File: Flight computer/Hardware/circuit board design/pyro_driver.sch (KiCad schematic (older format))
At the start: 7 parts, among them J4 Conn_01x06_Female, U5 LM2903, U6 Si7232DN

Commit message: worked on the silabs 4463 radio chip
- filled in the component values for TX matching and tx filtering
- filled in tentative values for RX LNA matching. Will have to verify
- swapped out XTAL and put in an RS Pro TCXO. Decoupled its powersupply.
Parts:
- R3: value 3.3 -> 3.3K
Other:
- moved on the sheet: R3, R4, R5, R6, U5A
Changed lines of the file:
@@
 $Descr A4 11693 8268
 encoding utf-8
-Sheet 7 7
+Sheet 6 7
 Title "Pyro drivers"
 Date "2019-08-26"
@@
 L Comparator:LM2903 U5
 U 1 1 5D6C6230
-P 3050 1550
-F 0 "U5" H 3050 1917 50  0000 C CNN
-F 1 "LM2903" H 3050 1826 50  0000 C CNN
-F 2 "" H 3050 1550 50  0001 C CNN
-F 3 "http://www.ti.com/lit/ds/symlink/lm393-n.pdf" H 3050 1550 50  0001 C CNN
-	1    3050 1550
+P 2700 1200
+F 0 "U5" H 2700 1567 50  0000 C CNN
+F 1 "LM2903" H 2700 1476 50  0000 C CNN
+F 2 "" H 2700 1200 50  0001 C CNN
+F 3 "http://www.ti.com/lit/ds/symlink/lm393-n.pdf" H 2700 1200 50  0001 C CNN
+	1    2700 1200
 	1    0    0    -1
 $EndComp
@@
 L Driver_FET:Si7232DN U6
 U 1 1 5D696EFB
-P 4400 1500
-F 0 "U6" H 4506 1046 50  0000 L CNN
-F 1 "Si7232DN" H 4506 955 50  0000 L CNN
-F 2 "Package_SO:Vishay_PowerPAK_1212-8_Dual" H 4250 1750 50  0001 C CNN
-F 3 "https://www.vishay.com/docs/68986/si7232dn.pdf" H 4400 1500 50  0001 C CNN
-	1    4400 1500
+P 4050 1150
+F 0 "U6" H 4156 696 50  0000 L CNN
+F 1 "Si7232DN" H 4156 605 50  0000 L CNN
+F 2 "Package_SO:Vishay_PowerPAK_1212-8_Dual" H 3900 1400 50  0001 C CNN
+F 3 "https://www.vishay.com/docs/68986/si7232dn.pdf" H 4050 1150 50  0001 C CNN
+	1    4050 1150
 	1    0    0    -1
 $EndComp
@@
 L power:GND #PWR024
 U 1 1 5D69AE81
-P 4400 2400
-F 0 "#PWR024" H 4400 2150 50  0001 C CNN
-F 1 "GND" H 4405 2227 50  0000 C CNN
-F 2 "" H 4400 2400 50  0001 C CNN
-F 3 "" H 4400 2400 50  0001 C CNN
-	1    4400 2400
-	1    0    0    -1
-$EndComp
-Wire Wire Line
-	4400 2400 4400 2150
+P 4050 2050
+F 0 "#PWR024" H 4050 1800 50  0001 C CNN
+F 1 "GND" H 4055 1877 50  0000 C CNN
+F 2 "" H 4050 2050 50  0001 C CNN
+F 3 "" H 4050 2050 50  0001 C CNN
+	1    4050 2050
+	1    0    0    -1
+$EndComp
+Wire Wire Line
+	4050 2050 4050 1800
 $Comp
 L Device:R R5
 U 1 1 5D6A50BE
-P 5050 1750
-F 0 "R5" V 5250 1750 50  0000 C CNN
-F 1 "100K" V 5150 1750 50  0000 C CNN
-F 2 "" V 4980 1750 50  0001 C CNN
-F 3 "~" H 5050 1750 50  0001 C CNN
-	1    5050 1750
+P 4700 1400
+F 0 "R5" V 4900 1400 50  0000 C CNN
+F 1 "100K" V 4800 1400 50  0000 C CNN
+F 2 "" V 4630 1400 50  0001 C CNN
+F 3 "~" H 4700 1400 50  0001 C CNN
+	1    4700 1400
 	0    1    1    0
 $EndComp
@@
 L Device:R R6
 U 1 1 5D6A6316
-P 5500 2200
-F 0 "R6" H 5570 2246 50  0000 L CNN
-F 1 "27K" H 5570 2155 50  0000 L CNN
-F 2 "" V 5430 2200 50  0001 C CNN
-F 3 "~" H 5500 2200 50  0001 C CNN
-	1    5500 2200
-	1    0    0    -1
-$EndComp
-Wire Wire Line
-	5200 1750 5500 1750
-Wire Wire Line
-	5500 2050 5500 1750
-Wire Wire Line
-	5500 2400 5500 2350
+P 5150 1850
+F 0 "R6" H 5220 1896 50  0000 L CNN
+F 1 "27K" H 5220 1805 50  0000 L CNN
+F 2 "" V 5080 1850 50  0001 C CNN
+F 3 "~" H 5150 1850 50  0001 C CNN
+	1    5150 1850
+	1    0    0    -1
+$EndComp
+Wire Wire Line
+	4850 1400 5150 1400
+Wire Wire Line
+	5150 1700 5150 1400
+Wire Wire Line
+	5150 2050 5150 2000
 $Comp
 L power:GND #PWR025
 U 1 1 5D6A67BF
-P 5500 2400
-F 0 "#PWR025" H 5500 2150 50  0001 C CNN
-F 1 "GND" H 5505 2227 50  0000 C CNN
-F 2 "" H 5500 2400 50  0001 C CNN
-F 3 "" H 5500 2400 50  0001 C CNN
-	1    5500 2400
-	1    0    0    -1
-$EndComp
-Wire Wire Line
-	4500 1750 4700 1750
-Wire Wire Line
-	4500 1650 4700 1650
-Wire Wire Line
-	4700 1750 4700 1650
-Connection ~ 4700 1750
-Wire Wire Line
-	4700 1750 4900 1750
-Connection ~ 4700 1650
-Wire Wire Line
-	4700 1650 6000 1650
-Connection ~ 5500 1750
-Wire Wire Line
-	5500 1750 6000 1750
-Text HLabel 6000 1750 2    50   Output ~ 0
+P 5150 2050
+F 0 "#PWR025" H 5150 1800 50  0001 C CNN
+F 1 "GND" H 5155 1877 50  0000 C CNN
+F 2 "" H 5150 2050 50  0001 C CNN
+F 3 "" H 5150 2050 50  0001 C CNN
+	1    5150 2050
+	1    0    0    -1
+$EndComp
+Wire Wire Line
+	4150 1400 4350 1400
+Wire Wire Line
+	4150 1300 4350 1300
+Wire Wire Line
+	4350 1400 4350 1300
+Connection ~ 4350 1400
+Wire Wire Line
+	4350 1400 4550 1400
+Connection ~ 4350 1300
+Wire Wire Line
+	4350 1300 5650 1300
+Connection ~ 5150 1400
+Wire Wire Line
+	5150 1400 5650 1400
+Text HLabel 5650 1400 2    50   Output ~ 0
 sense_fet_a
-Text Label 6000 1650 0    50   ~ 0
+Text Label 5650 1300 0    50   ~ 0
 fet_a
 Wire Wire Line
-	3350 1550 3800 1550
-Wire Wire Line
-	3800 1550 3800 1950
-Wire Wire Line
-	3800 1950 4100 1950
-Wire Wire Line
-	3800 1950 3500 1950
-Connection ~ 3800 1950
-Wire Wire Line
-	3000 1950 3000 2100
-Connection ~ 3000 1950
-Wire Wire Line
-	3000 1950 2250 1950
+	3000 1200 3450 1200
+Wire Wire Line
+	3450 1200 3450 1600
+Wire Wire Line
+	3450 1600 3750 1600
+Wire Wire Line
+	3450 1600 3150 1600
+Connection ~ 3450 1600
+Wire Wire Line
+	2650 1600 2650 1750
+Connection ~ 2650 1600
+Wire Wire Line
+	2650 1600 1900 1600
 $Comp
 L power:GND #PWR023
 U 1 1 5D6AF664
-P 3000 2500
-F 0 "#PWR023" H 3000 2250 50  0001 C CNN
-F 1 "GND" H 3005 2327 50  0000 C CNN
-F 2 "" H 3000 2500 50  0001 C CNN
-F 3 "" H 3000 2500 50  0001 C CNN
-	1    3000 2500
+P 2650 2150
+F 0 "#PWR023" H 2650 1900 50  0001 C CNN
+F 1 "GND" H 2655 1977 50  0000 C CNN
+F 2 "" H 2650 2150 50  0001 C CNN
+F 3 "" H 2650 2150 50  0001 C CNN
+	1    2650 2150
 	1    0    0    -1
 $EndComp
@@
 L Device:R R3
 U 1 1 5D6AFE1F
-P 3000 2250
-F 0 "R3" H 3070 2296 50  0000 L CNN
-F 1 "3.3" H 3070 2205 50  0000 L CNN
-F 2 "" V 2930 2250 50  0001 C CNN
-F 3 "~" H 3000 2250 50  0001 C CNN
-	1    3000 2250
-	1    0    0    -1
-$EndComp
-Wire Wire Line
-	3000 2400 3000 2500
+P 2650 1900
+F 0 "R3" H 2720 1946 50  0000 L CNN
+F 1 "3.3K" H 2720 1855 50  0000 L CNN
+F 2 "" V 2580 1900 50  0001 C CNN
+F 3 "~" H 2650 1900 50  0001 C CNN
+	1    2650 1900
+	1    0    0    -1
+$EndComp
+Wire Wire Line
+	2650 2050 2650 2150
 $Comp
 L Device:R R4
 U 1 1 5D6B06F6
-P 3350 1950
-F 0 "R4" V 3143 1950 50  0000 C CNN
-F 1 "100" V 3234 1950 50  0000 C CNN
-F 2 "" V 3280 1950 50  0001 C CNN
-F 3 "~" H 3350 1950 50  0001 C CNN
-	1    3350 1950
+P 3000 1600
+F 0 "R4" V 2793 1600 50  0000 C CNN
+F 1 "100" V 2884 1600 50  0000 C CNN
+F 2 "" V 2930 1600 50  0001 C CNN
+F 3 "~" H 3000 1600 50  0001 C CNN
+	1    3000 1600
 	0    1    1    0
 $EndComp
 Wire Wire Line
-	3200 1950 3000 1950
-Text HLabel 2250 1950 0    50   Output ~ 0
+	2850 1600 2650 1600
+Text HLabel 1900 1600 0    50   Output ~ 0
 fire_a
 $Comp
@@
 	1    0    0    -1
 $EndComp
-NoConn ~ 2750 1650
-NoConn ~ 2750 1450
+NoConn ~ 2400 1300
+NoConn ~ 2400 1100
 NoConn ~ 1900 3900
 NoConn ~ 1900 4000

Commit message: Work in progress for Telemetry Radio
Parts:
- U6: symbol Driver_FET:Si7232DN -> circuit-board-design-rescue:Si7232DN-Driver_FET
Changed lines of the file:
@@
 $EndComp
 $Comp
-L Driver_FET:Si7232DN U6
+L circuit-board-design-rescue:Si7232DN-Driver_FET U6
 U 1 1 5D696EFB
 P 4050 1150
+AR Path="/5D696EFB" Ref="U6"  Part="1"
+AR Path="/5D6468D5/5D696EFB" Ref="U6"  Part="1"
 F 0 "U6" H 4156 696 50  0000 L CNN
 F 1 "Si7232DN" H 4156 605 50  0000 L CNN

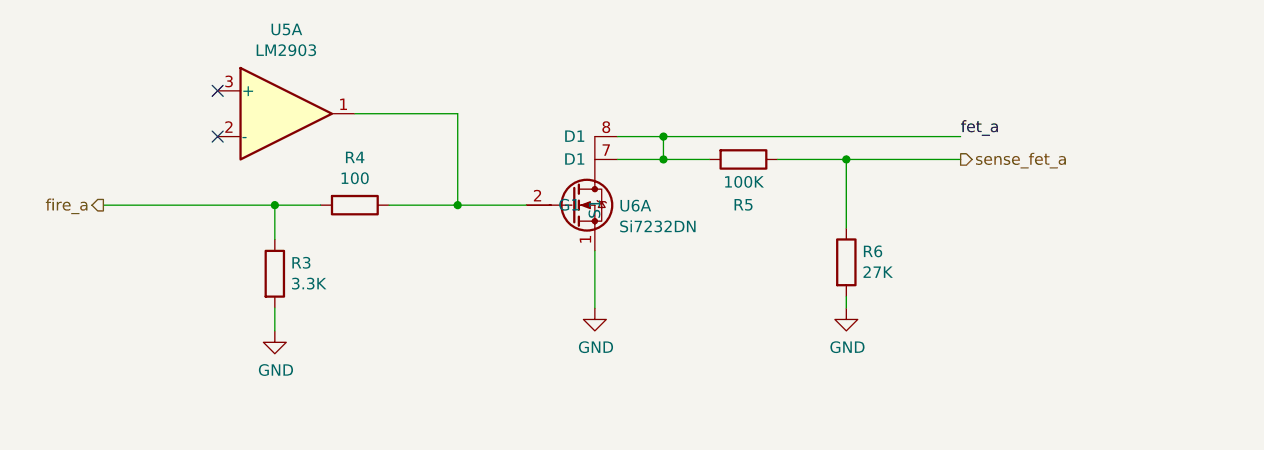
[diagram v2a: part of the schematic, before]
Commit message: changed the SPI flash chip
-changed to Winbond W74M64FV 64Mbit flash chip to run on 3.3V. Changed schematic symbol and foot print.
- changed the names of hierarchical labels for the pyros
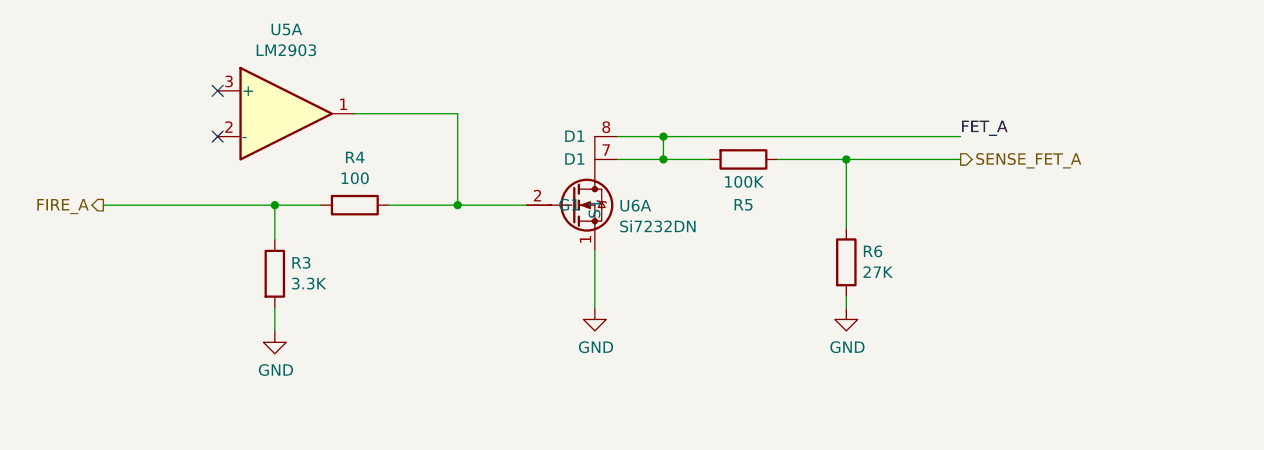
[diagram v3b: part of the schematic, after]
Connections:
- net fet_a renamed FET_A
- net fire_a renamed FIRE_A
- net sense_fet_a renamed SENSE_FET_A
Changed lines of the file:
@@
 	5150 1400 5650 1400
 Text HLabel 5650 1400 2    50   Output ~ 0
-sense_fet_a
+SENSE_FET_A
 Text Label 5650 1300 0    50   ~ 0
-fet_a
+FET_A
 Wire Wire Line
 	3000 1200 3450 1200
@@
 	2850 1600 2650 1600
 Text HLabel 1900 1600 0    50   Output ~ 0
-fire_a
+FIRE_A
 $Comp
 L power:GND #PWR027

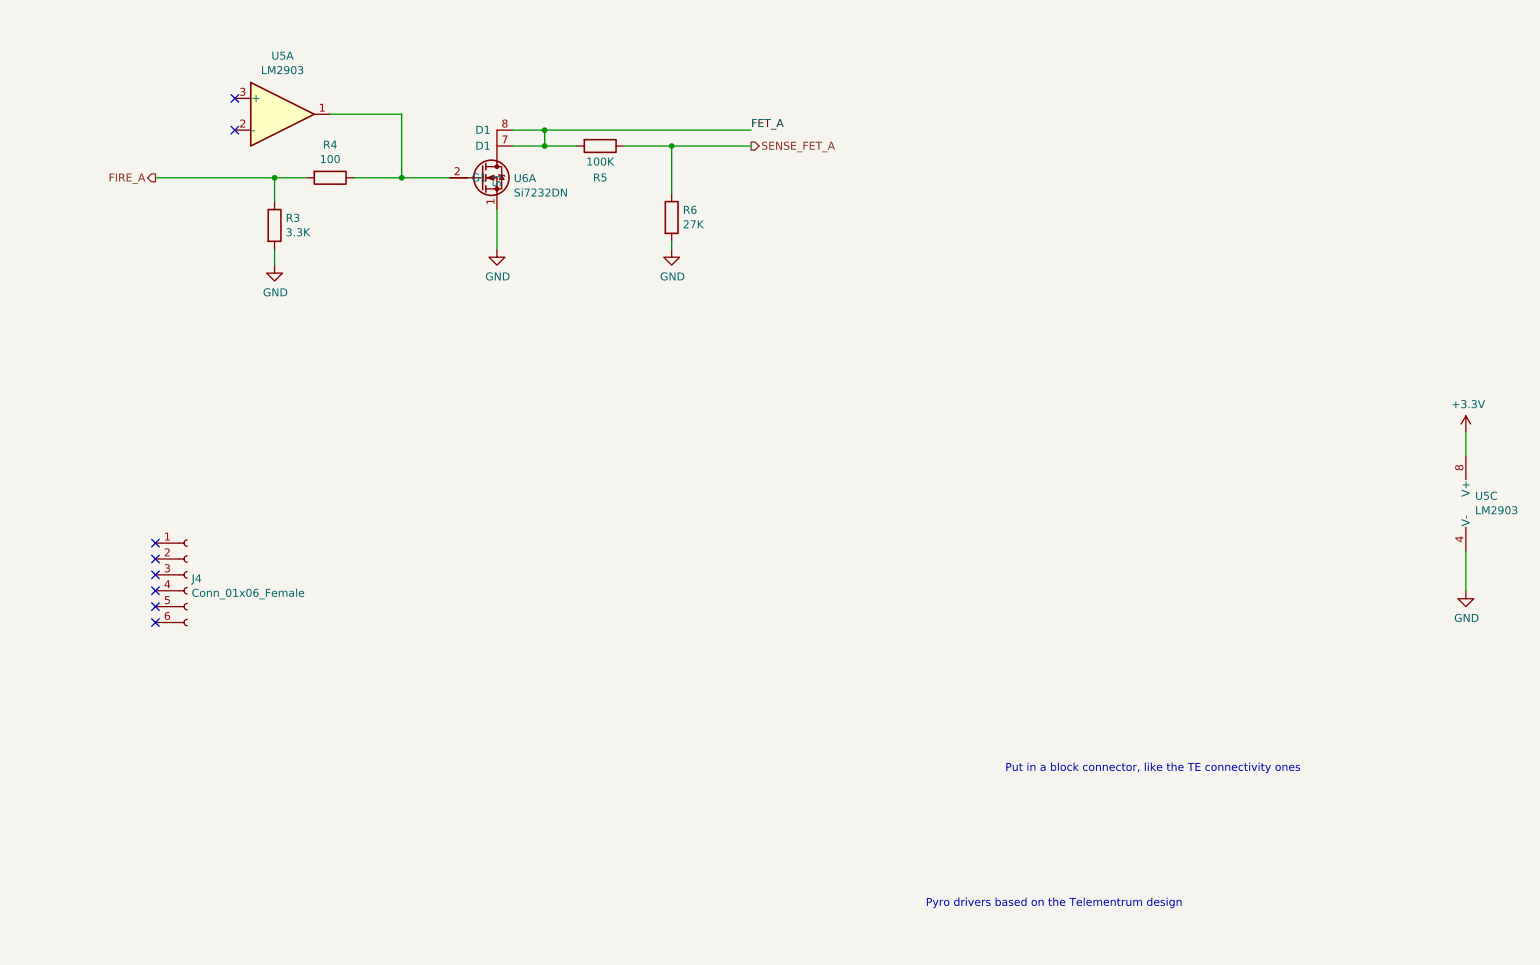
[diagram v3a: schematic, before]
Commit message: created net list for first time
-changed SAML21 to J variant7
-filled in foot prints for all components exept comparator
-changed the footprints of ICSS pico tracker to a local copy
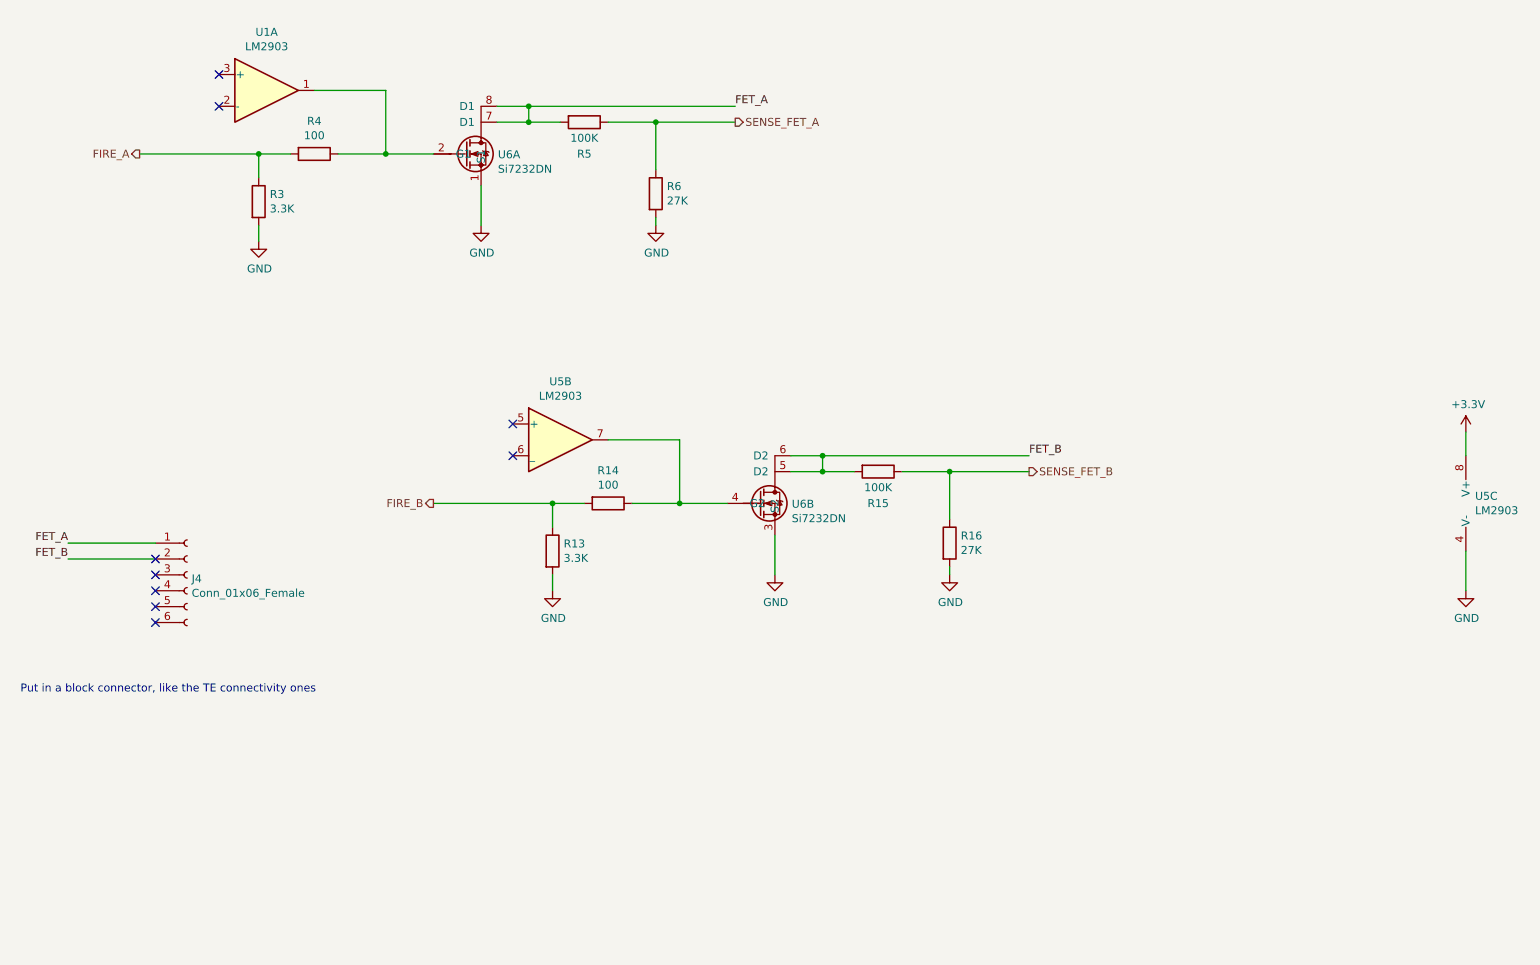
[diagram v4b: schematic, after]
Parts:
- added R13: 3.3K, Resistor_SMD:R_0603_1608Metric, symbol Device:R
- added R14: 100, Resistor_SMD:R_0603_1608Metric, symbol Device:R
- added R15: 100K, Resistor_SMD:R_0603_1608Metric, symbol Device:R
- added R16: 27K, Resistor_SMD:R_0603_1608Metric, symbol Device:R
- added unit 2 of U5
- added unit 2 of U6
- R3, R4, R5, R6: footprint (none) -> Resistor_SMD:R_0603_1608Metric
- renumbered U5 to U1
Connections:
- net FET_A: now also J4.1 (Pin_1)
- net GND: now also R13.2, R16.2, U6.3 (S2)
- net FET_B: now reaches J4.2 (Pin_2)
- net FET_B: now also R15.2, U6.5 (D2), U6.6 (D2)
- new net: R14.1, U5.7, U6.4 (G2)
- new net FIRE_B: R13.1, R14.2
- new net SENSE_FET_B: R15.1, R16.1
- no-connect marks 8 -> 9
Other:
- note removed: "Pyro drivers based on the Telementrum design\n"
- moved on the sheet: R3, R4, R5, R6, U1A, U6A
